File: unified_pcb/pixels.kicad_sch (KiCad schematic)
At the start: 291 parts

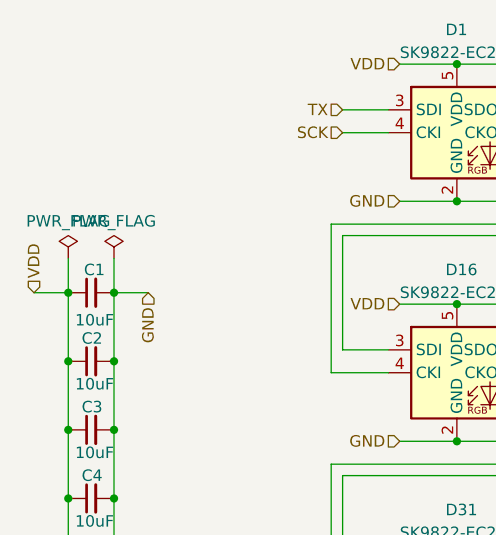
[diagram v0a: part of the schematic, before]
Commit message: lots of layout improves, ERC fixes
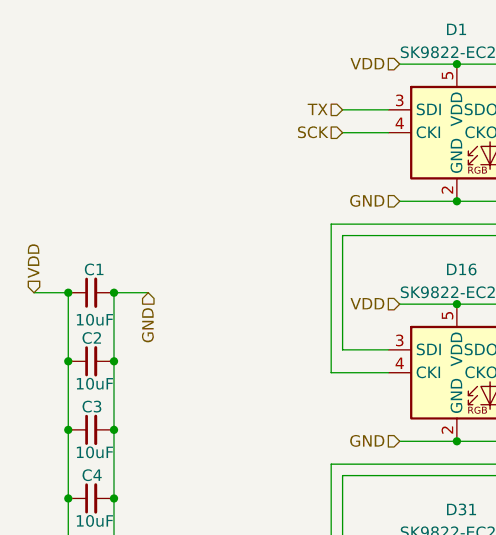
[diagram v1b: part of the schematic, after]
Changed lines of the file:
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@@
 	(wire
 		(pts
-			(xy 54.61 48.26) (xy 54.61 52.07)
-		)
-		(stroke
-			(width 0)
-			(type default)
-		)
-	)
-	(wire
-		(pts
 			(xy 83.82 444.5) (xy 83.82 461.01)
 		)
@@
 	(wire
 		(pts
-			(xy 59.69 48.26) (xy 59.69 52.07)
-		)
-		(stroke
-			(width 0)
-			(type default)
-		)
-	)
-	(wire
-		(pts
 			(xy 321.31 378.46) (xy 321.31 392.43)
 		)
@@
 	)
 	(symbol
-		(lib_id "power:PWR_FLAG")
-		(at 59.69 48.26 0)
-		(unit 1)
-		(exclude_from_sim no)
-		(in_bom yes)
-		(on_board yes)
-		(dnp no)
-		(fields_autoplaced yes)
-		(property "Reference" "#FLG02"
-			(at 59.69 46.355 0)
-			(effects
-				(font
-					(size 1.27 1.27)
-				)
-				(hide yes)
-			)
-		)
-		(property "Value" "PWR_FLAG"
-			(at 59.69 44.1269 0)
-			(effects
-				(font
-					(size 1.27 1.27)
-				)
-			)
-		)
-		(property "Footprint" ""
-			(at 59.69 48.26 0)
-			(effects
-				(font
-					(size 1.27 1.27)
-				)
-				(hide yes)
-			)
-		)
-		(property "Datasheet" "~"
-			(at 59.69 48.26 0)
-			(effects
-				(font
-					(size 1.27 1.27)
-				)
-				(hide yes)
-			)
-		)
-		(property "Description" ""
-			(at 59.69 48.26 0)
-			(effects
-				(font
-					(size 1.27 1.27)
-				)
-				(hide yes)
-			)
-		)
-		(pin "1"
-		)
-		(instances
-			(project "unified_pcb"
-				(path "/5ec870f3-18d6-4ff4-bc31-ac41fb778ddb/b1c8d1d8-e566-4e62-90b7-cb368edd71ad"
-					(reference "#FLG02")
-					(unit 1)
-				)
-			)
-		)
-	)
-	(symbol
 		(lib_id "motionhexa:LED-SK9822-EC20")
 		(at 234.95 34.29 0)
@@
 					(unit 1)
 				)
-			)
-		)
-	)
-	(symbol
-		(lib_id "power:PWR_FLAG")
-		(at 54.61 48.26 0)
-		(unit 1)
-		(exclude_from_sim no)
-		(in_bom yes)
-		(on_board yes)
-		(dnp no)
-		(fields_autoplaced yes)
-		(property "Reference" "#FLG01"
-			(at 54.61 46.355 0)
-			(effects
-				(font
-					(size 1.27 1.27)
-				)
-				(hide yes)
-			)
-		)
-		(property "Value" "PWR_FLAG"
-			(at 54.61 44.1269 0)
-			(effects
-				(font
-					(size 1.27 1.27)
-				)
-			)
-		)
-		(property "Footprint" ""
-			(at 54.61 48.26 0)
-			(effects
-				(font
-					(size 1.27 1.27)
-				)
-				(hide yes)
-			)
-		)
-		(property "Datasheet" "~"
-			(at 54.61 48.26 0)
-			(effects
-				(font
-					(size 1.27 1.27)
-				)
-				(hide yes)
-			)
-		)
-		(property "Description" ""
-			(at 54.61 48.26 0)
-			(effects
-				(font
-					(size 1.27 1.27)
-				)
-				(hide yes)
-			)
-		)
-		(pin "1"
-		)
-		(instances
-			(project "unified_pcb"
-				(path "/5ec870f3-18d6-4ff4-bc31-ac41fb778ddb/b1c8d1d8-e566-4e62-90b7-cb368edd71ad"
-					(reference "#FLG01")
-					(unit 1)
-				)

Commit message: ERC fixes
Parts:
- D1, D10, D100, D101, D102, D103, D104, D105, D106, D107, D108, D109, D11, D110, D111, D112, D113, D114, D115, D116, D117, D118, D119, D12, D120, D121, D122, D123, D124, D125, D126, D127, D128, D129, D13, D130, D131, D132, D133, D134, D135, D136, D137, D138, D139, D14, D140, D141, D142, D143, D144, D145, D146, D147, D148, D149, D15, D150, D151, D152, D153, D154, D155, D156, D157, D158, D159, D16, D160, D161, D162, D163, D164, D165, D166, D167, D168, D169, D17, D170, D171, D172, D173, D174, D175, D176, D177, D178, D179, D18, D180, D181, D182, D183, D184, D185, D186, D187, D188, D189, D19, D190, D191, D192, D193, D194, D195, D196, D197, D198, D199, D2, D20, D200, D201, D202, D203, D204, D205, D206, D207, D208, D209, D21, D210, D211, D212, D213, D214, D215, D216, D217, D218, D219, D22, D220, D221, D222, D223, D224, D225, D226, D227, D228, D229, D23, D230, D231, D232, D233, D234, D235, D236, D237, D238, D239, D24, D240, D241, D242, D243, D244, D245, D246, D247, D248, D249, D25, D250, D251, D252, D253, D254, D255, D256, D257, D258, D259, D26, D260, D261, D262, D263, D264, D265, D266, D267, D268, D269, D27, D270, D271, D28, D29, D3, D30, D31, D32, D33, D34, D35, D36, D37, D38, D39, D4, D40, D41, D42, D43, D44, D45, D46, D47, D48, D49, D5, D50, D51, D52, D53, D54, D55, D56, D57, D58, D59, D6, D60, D61, D62, D63, D64, D65, D66, D67, D68, D69, D7, D70, D71, D72, D73, D74, D75, D76, D77, D78, D79, D8, D80, D81, D82, D83, D84, D85, D86, D87, D88, D89, D9, D90, D91, D92, D93, D94, D95, D96, D97, D98, D99: Designation (none) -> SK9822-EC20; LCSC (none) -> C2909059
